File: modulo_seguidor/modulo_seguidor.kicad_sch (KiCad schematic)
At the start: 30 parts, among them J1 Battery, J2 Motor A Entradas, J3 Motor B Entradas, J4 Motor IZQ Arduino OUTPUT, J5 Motor DER Arduino OUTPUT, J6 puerto sensores, M1 Motor_IZQ, M2 Motor_DER, SW1 SW_Push, SW2 SW_Nidec_CAS-120A1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

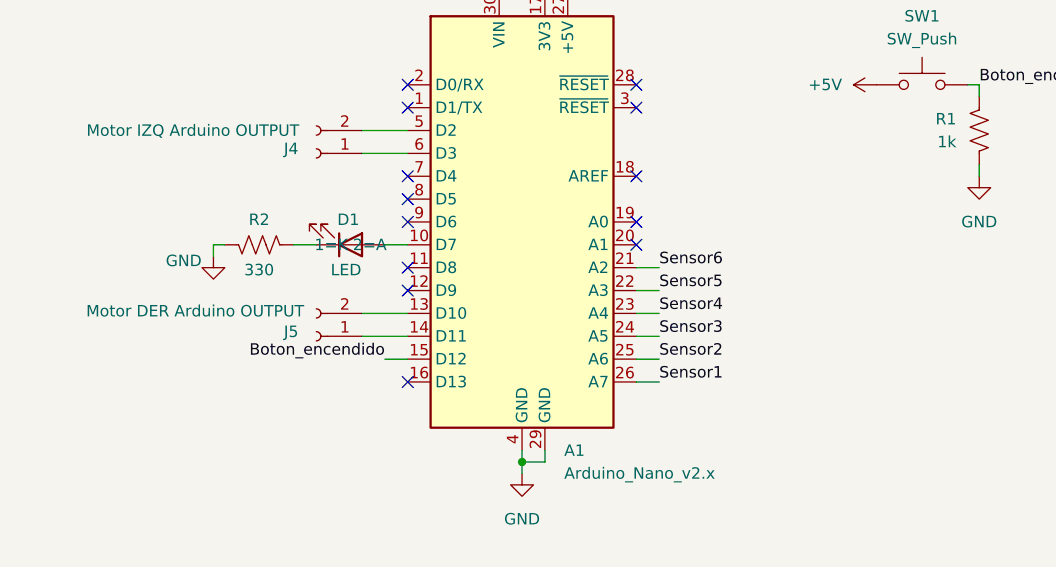
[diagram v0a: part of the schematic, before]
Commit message: reactor(modulo-seguidor): Modifico las pistas de VCC
Los diodos de ambos motores ahora no son simétricos
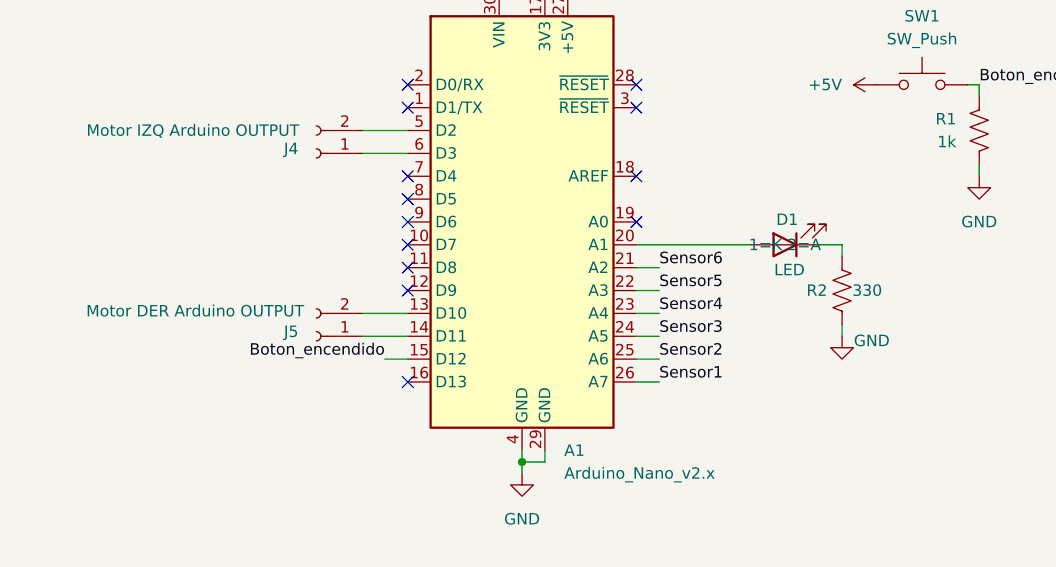
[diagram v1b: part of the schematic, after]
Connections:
- net GND: now also R2.2; no longer R2.1
- net at D1.1 (K): now also R2.1; no longer R2.2
- net at D1.2 (A): now also A1.20 (A1); no longer A1.10 (D7)
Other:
- moved on the sheet: D1, R2
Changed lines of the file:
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@@
 	)
 	(no_connect
-		(at 158.75 64.77)
+		(at 133.35 64.77)
 	)
 	(no_connect
@@
 	(wire
 		(pts
-			(xy 130.81 64.77) (xy 133.35 64.77)
-		)
-		(stroke
-			(width 0)
-			(type default)
-		)
-	)
-	(wire
-		(pts
 			(xy 36.83 36.83) (xy 36.83 33.02)
 		)
@@
 	(wire
 		(pts
-			(xy 111.76 64.77) (xy 111.76 66.04)
+			(xy 181.61 73.66) (xy 181.61 74.93)
 		)
 		(stroke
@@
 	(wire
 		(pts
-			(xy 123.19 64.77) (xy 120.65 64.77)
+			(xy 181.61 64.77) (xy 181.61 66.04)
+		)
+		(stroke
+			(width 0)
+			(type default)
+		)
+	)
+	(wire
+		(pts
+			(xy 179.07 64.77) (xy 181.61 64.77)
 		)
 		(stroke
@@
 	(wire
 		(pts
+			(xy 158.75 64.77) (xy 171.45 64.77)
+		)
+		(stroke
+			(width 0)
+			(type default)
+		)
+	)
+	(wire
+		(pts
 			(xy 36.83 26.67) (xy 45.72 26.67)
 		)
@@
 	(wire
 		(pts
-			(xy 113.03 64.77) (xy 111.76 64.77)
-		)
-		(stroke
-			(width 0)
-			(type default)
-		)
-	)
-	(wire
-		(pts
 			(xy 113.03 154.94) (xy 114.3 154.94)
 		)
@@
 	(symbol
 		(lib_id "Device:LED")
-		(at 127 64.77 0)
-		(mirror x)
+		(at 175.26 64.77 180)
 		(unit 1)
 		(exclude_from_sim no)
@@
 		(dnp no)
 		(property "Reference" "D1"
-			(at 126.746 61.976 0)
+			(at 175.514 61.976 0)
 			(effects
 				(font
@@
 		)
 		(property "Value" "LED"
-			(at 126.492 67.564 0)
+			(at 175.768 67.564 0)
 			(effects
 				(font
@@
 		)
 		(property "Footprint" "LED_THT:LED_D5.0mm"
-			(at 127 64.77 0)
+			(at 175.26 64.77 0)
 			(effects
 				(font
@@
 		)
 		(property "Datasheet" "~"
-			(at 127 64.77 0)
+			(at 175.26 64.77 0)
 			(effects
 				(font
@@
 		)
 		(property "Description" "Light emitting diode"
-			(at 127 64.77 0)
+			(at 175.26 64.77 0)
 			(effects
 				(font
@@
 		)
 		(property "Sim.Pins" "1=K 2=A"
-			(at 127 64.77 0)
+			(at 175.26 64.77 0)
 			(effects
 				(font
@@
 	(symbol
 		(lib_id "Device:R_US")
-		(at 116.84 64.77 90)
-		(mirror x)
+		(at 181.61 69.85 0)
 		(unit 1)
 		(exclude_from_sim no)
@@
 		(dnp no)
 		(property "Reference" "R2"
-			(at 116.84 61.976 90)
+			(at 178.816 69.85 0)
 			(effects
 				(font
@@
 		)
 		(property "Value" "330"
-			(at 116.84 67.564 90)
+			(at 184.404 69.85 0)
 			(effects
 				(font
@@
 		)
 		(property "Footprint" "Resistor_SMD:R_1206_3216Metric_Pad1.30x1.75mm_HandSolder"
-			(at 117.094 65.786 90)
+			(at 182.626 70.104 90)
 			(effects
 				(font
@@
 		)
 		(property "Datasheet" "~"
-			(at 116.84 64.77 0)
+			(at 181.61 69.85 0)
 			(effects
 				(font
@@
 		)
 		(property "Description" "Resistor, US symbol"
-			(at 116.84 64.77 0)
+			(at 181.61 69.85 0)
 			(effects
 				(font
@@
 	(symbol
 		(lib_id "power:GND")
-		(at 111.76 66.04 0)
-		(mirror y)
+		(at 181.61 74.93 0)
 		(unit 1)
 		(exclude_from_sim no)
@@
 		(dnp no)
 		(property "Reference" "#PWR06"
-			(at 111.76 72.39 0)
+			(at 181.61 81.28 0)
 			(effects
 				(font
@@
 		)
 		(property "Value" "GND"
-			(at 108.458 66.548 0)
+			(at 184.912 75.438 0)
 			(effects
 				(font
@@
 		)
 		(property "Footprint" ""
-			(at 111.76 66.04 0)
+			(at 181.61 74.93 0)
 			(effects
 				(font
@@
 		)
 		(property "Datasheet" ""
-			(at 111.76 66.04 0)
+			(at 181.61 74.93 0)
 			(effects
 				(font
@@
 		)
 		(property "Description" "Power symbol creates a global label with name \"GND\" , ground"
-			(at 111.76 66.04 0)
+			(at 181.61 74.93 0)
 			(effects
 				(font

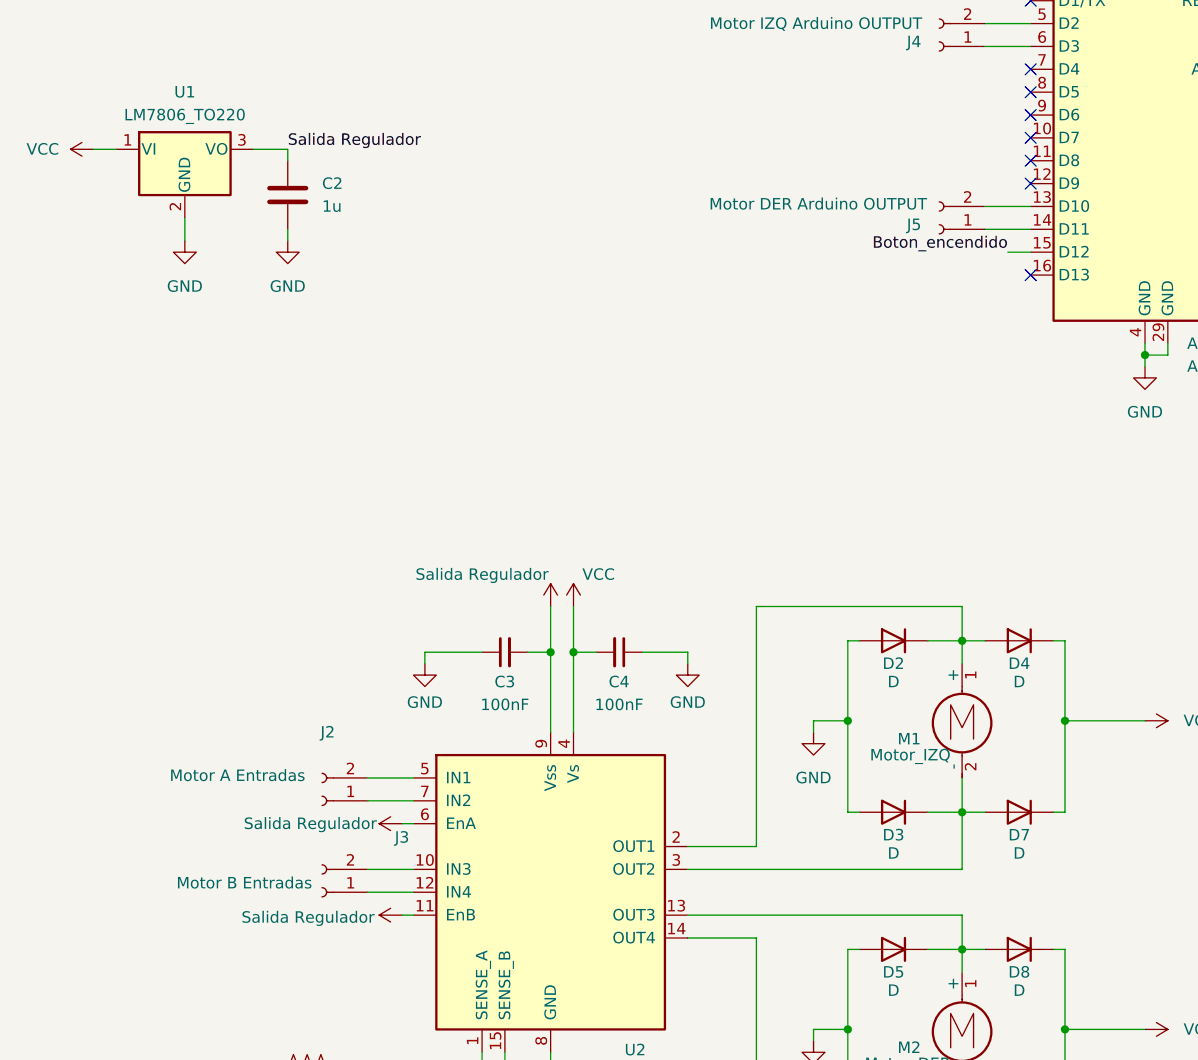
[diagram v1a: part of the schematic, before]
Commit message: refactor(modulo-seguidor): Elimino jumpers de entradas de un motor del puente H
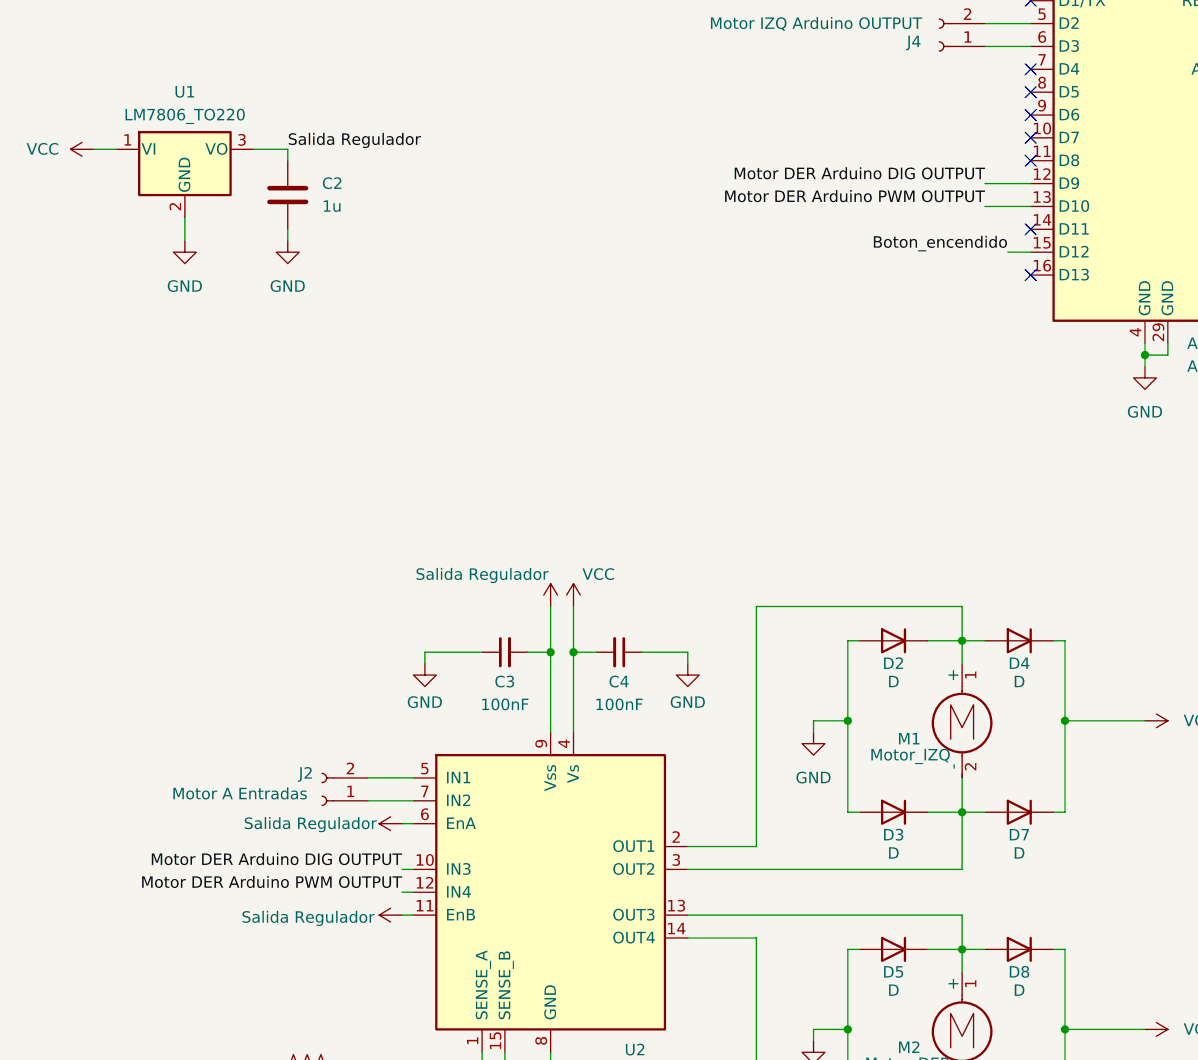
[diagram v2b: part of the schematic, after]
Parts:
- removed J3: Motor B Entradas, Connector_Molex:Molex_KK-254_AE-6410-02A_1x02_P2.54mm_Vertical, symbol Connector:Conn_01x02_Socket
- removed J5: Motor DER Arduino OUTPUT, Connector_Molex:Molex_KK-254_AE-6410-02A_1x02_P2.54mm_Vertical, symbol Connector:Conn_01x02_Socket
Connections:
- net Motor DER Arduino PWM OUTPUT: now reaches A1.13 (D10)
- net Motor DER Arduino PWM OUTPUT: now also U2.12 (IN4)
- net Motor DER Arduino DIG OUTPUT: now reaches A1.12 (D9)
- net Motor DER Arduino DIG OUTPUT: now also U2.10 (IN3)
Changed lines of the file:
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@@
 	)
 	(no_connect
-		(at 133.35 69.85)
+		(at 133.35 74.93)
 	)
 	(no_connect
@@
 	(wire
 		(pts
-			(xy 59.69 146.05) (xy 64.77 146.05)
-		)
-		(stroke
-			(width 0)
-			(type default)
-		)
-	)
-	(wire
-		(pts
 			(xy 240.03 49.53) (xy 240.03 50.8)
 		)
@@
 	(wire
 		(pts
+			(xy 63.5 148.59) (xy 64.77 148.59)
+		)
+		(stroke
+			(width 0)
+			(type default)
+		)
+	)
+	(wire
+		(pts
 			(xy 113.03 120.65) (xy 113.03 129.54)
 		)
@@
 	(wire
 		(pts
-			(xy 59.69 148.59) (xy 64.77 148.59)
+			(xy 137.16 120.65) (xy 135.89 120.65)
 		)
 		(stroke
@@
 	(wire
 		(pts
-			(xy 137.16 120.65) (xy 135.89 120.65)
+			(xy 196.85 55.88) (xy 196.85 57.15)
 		)
 		(stroke
@@
 	(wire
 		(pts
-			(xy 196.85 55.88) (xy 196.85 57.15)
+			(xy 50.8 66.04) (xy 50.8 67.31)
 		)
 		(stroke
@@
 	(wire
 		(pts
-			(xy 50.8 66.04) (xy 50.8 67.31)
+			(xy 161.29 77.47) (xy 158.75 77.47)
 		)
 		(stroke
@@
 	(wire
 		(pts
-			(xy 161.29 77.47) (xy 158.75 77.47)
+			(xy 237.49 36.83) (xy 241.3 36.83)
 		)
 		(stroke
@@
 	(wire
 		(pts
-			(xy 237.49 36.83) (xy 241.3 36.83)
+			(xy 113.03 154.94) (xy 114.3 154.94)
 		)
 		(stroke
@@
 	(wire
 		(pts
-			(xy 113.03 154.94) (xy 114.3 154.94)
+			(xy 50.8 74.93) (xy 50.8 76.2)
 		)
 		(stroke
@@
 	(wire
 		(pts
-			(xy 50.8 74.93) (xy 50.8 76.2)
+			(xy 63.5 146.05) (xy 64.77 146.05)
 		)
 		(stroke
@@
 	(wire
 		(pts
-			(xy 128.27 74.93) (xy 133.35 74.93)
+			(xy 128.27 69.85) (xy 133.35 69.85)
 		)
 		(stroke
@@
 		)
 	)
+	(label "Motor DER Arduino DIG OUTPUT"
+		(at 63.5 146.05 180)
+		(effects
+			(font
+				(size 1.27 1.27)
+			)
+			(justify right bottom)
+		)
+	)
+	(label "Motor DER Arduino DIG OUTPUT"
+		(at 128.27 69.85 180)
+		(effects
+			(font
+				(size 1.27 1.27)
+			)
+			(justify right bottom)
+		)
+	)
 	(label "Sensor1"
 		(at 161.29 80.01 0)
@@
 		)
 	)
+	(label "Motor DER Arduino PWM OUTPUT"
+		(at 128.27 72.39 180)
+		(effects
+			(font
+				(size 1.27 1.27)
+			)
+			(justify right bottom)
+		)
+	)
 	(label "Sensor3"
 		(at 161.29 74.93 0)
@@
 		)
 	)
+	(label "Motor DER Arduino PWM OUTPUT"
+		(at 63.5 148.59 180)
+		(effects
+			(font
+				(size 1.27 1.27)
+			)
+			(justify right bottom)
+		)
+	)
 	(label "Sensor6"
 		(at 161.29 67.31 0)
@@
 		(dnp no)
 		(property "Reference" "J2"
-			(at 55.245 130.81 0)
+			(at 52.832 135.382 0)
 			(effects
 				(font
@@
 		)
 		(property "Value" "Motor A Entradas"
-			(at 45.212 135.636 0)
+			(at 45.466 137.668 0)
 			(effects
 				(font
@@
 	)
 	(symbol
-		(lib_id "Connector:Conn_01x02_Socket")
-		(at 123.19 74.93 180)
-		(unit 1)
-		(exclude_from_sim no)
-		(in_bom yes)
-		(on_board yes)
-		(dnp no)
-		(property "Reference" "J5"
-			(at 120.396 74.422 0)
-			(effects
-				(font
-					(size 1.27 1.27)
-				)
-			)
-		)
-		(property "Value" "Motor DER Arduino OUTPUT"
-			(at 109.728 72.136 0)
-			(effects
-				(font
-					(size 1.27 1.27)
-				)
-			)
-		)
-		(property "Footprint" "Connector_Molex:Molex_KK-254_AE-6410-02A_1x02_P2.54mm_Vertical"
-			(at 123.19 74.93 0)
-			(effects
-				(font
-					(size 1.27 1.27)
-				)
-				(hide yes)
-			)
-		)
-		(property "Datasheet" "~"
-			(at 123.19 74.93 0)
-			(effects
-				(font
-					(size 1.27 1.27)
-				)
-				(hide yes)
-			)
-		)
-		(property "Description" "Generic connector, single row, 01x02, script generated"
-			(at 123.19 74.93 0)
-			(effects
-				(font
-					(size 1.27 1.27)
-				)
-				(hide yes)
-			)
-		)
-		(pin "1"
-		)
-		(pin "2"
-		)
-		(instances
-			(project "modulo_seguidor"
-				(path "/506ff443-80b5-4c22-9098-af8632a73945"
-					(reference "J5")
-					(unit 1)
-				)
-			)
-		)
-	)
-	(symbol
 		(lib_id "Device:R_US")
 		(at 53.34 167.64 270)
@@
 					(unit 1)
 				)
-			)
-		)
-	)
-	(symbol
-		(lib_id "Connector:Conn_01x02_Socket")
-		(at 54.61 148.59 180)
-		(unit 1)
-		(exclude_from_sim no)
-		(in_bom yes)
-		(on_board yes)
-		(dnp no)
-		(property "Reference" "J3"
-			(at 63.5 142.494 0)
-			(effects
-				(font
-					(size 1.27 1.27)
-				)
-			)
-		)
-		(property "Value" "Motor B Entradas"
-			(at 45.974 147.574 0)
-			(effects
-				(font
-					(size 1.27 1.27)
-				)
-			)
-		)
-		(property "Footprint" "Connector_Molex:Molex_KK-254_AE-6410-02A_1x02_P2.54mm_Vertical"
-			(at 54.61 148.59 0)
-			(effects
-				(font
-					(size 1.27 1.27)
-				)
-				(hide yes)
-			)
-		)
-		(property "Datasheet" "~"
-			(at 54.61 148.59 0)
-			(effects
-				(font
-					(size 1.27 1.27)
-				)
-				(hide yes)
-			)
-		)
-		(property "Description" "Generic connector, single row, 01x02, script generated"
-			(at 54.61 148.59 0)
-			(effects
-				(font
-					(size 1.27 1.27)
-				)
-				(hide yes)
-			)
-		)
-		(pin "1"
-		)
-		(pin "2"
-		)
-		(instances
-			(project "modulo_seguidor"
-				(path "/506ff443-80b5-4c22-9098-af8632a73945"
-					(reference "J3")
-					(unit 1)
-				)
